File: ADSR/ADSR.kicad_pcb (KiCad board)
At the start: 2 copper layers, 44 parts, among them J1 Panel, J2 Power, Q1 BC547, Q2 BC547, Q3 BC547, U1 LM358, U2 ICM7555

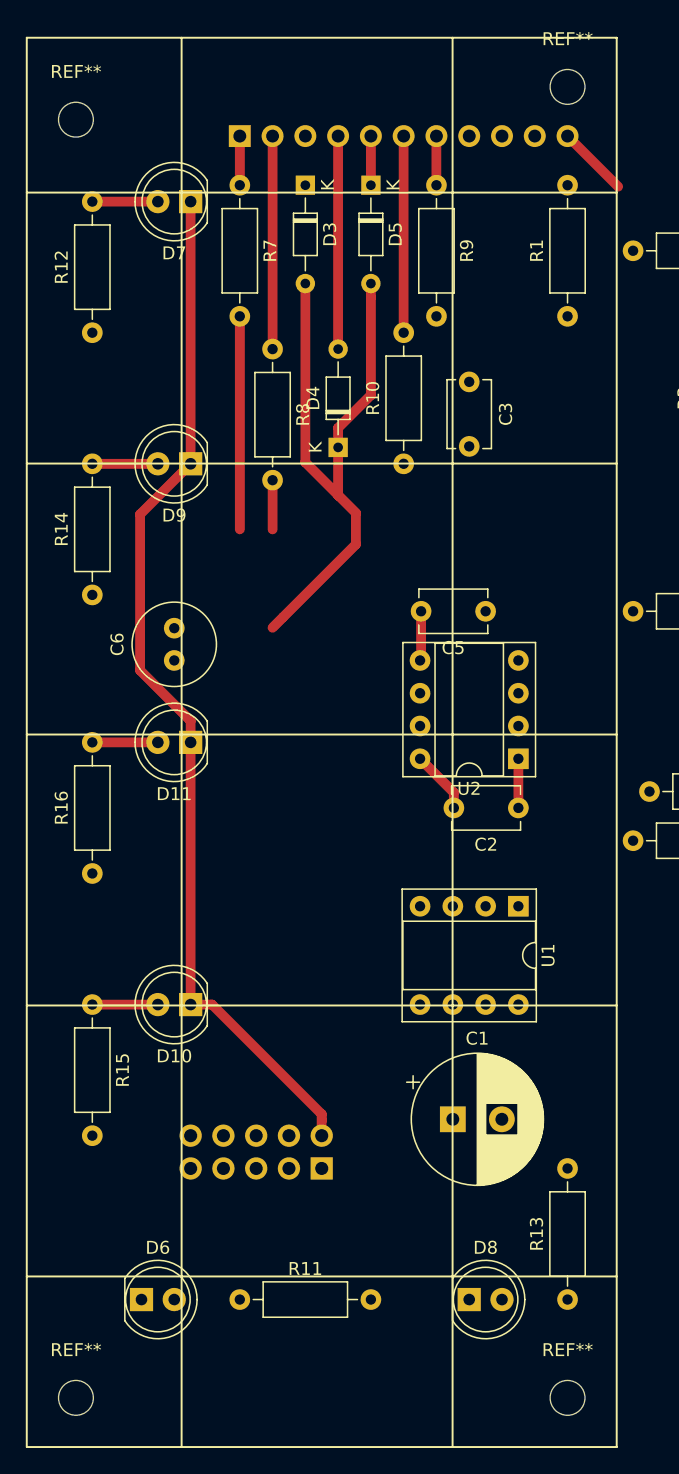
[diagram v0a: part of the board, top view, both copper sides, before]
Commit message: update ADSR footprints
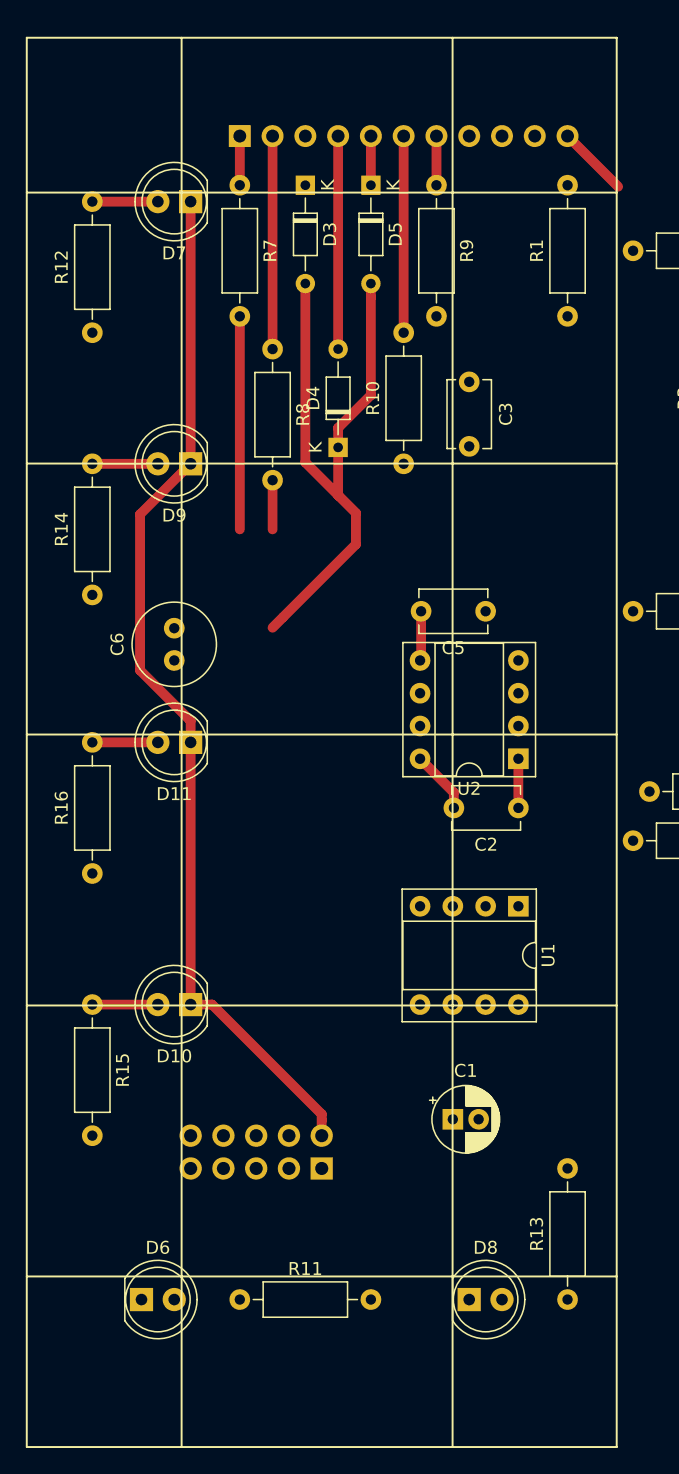
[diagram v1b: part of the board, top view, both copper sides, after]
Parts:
- removed REF** (x4): MountingHole_2.7mm, MountingHole:MountingHole_2.7mm
- C1: footprint Capacitor_THT:CP_Radial_D10.0mm_P3.80mm -> Capacitor_THT:CP_Radial_D5.0mm_P2.00mm
- C6: value 4.7u -> 4u7
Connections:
- C6 pad 1: GND -> Net-(C6-Pad1)
- C6 pad 2: Net-(C6-Pad2) -> GND
- D3 pad 2: Net-(C6-Pad2) -> Net-(C6-Pad1)
- D4 pad 1: Net-(C6-Pad2) -> Net-(C6-Pad1)
- D5 pad 2: Net-(C6-Pad2) -> Net-(C6-Pad1)
- U1 pad 3: Net-(C6-Pad2) -> Net-(C6-Pad1)
- U2 pad 6: Net-(C6-Pad2) -> Net-(C6-Pad1)
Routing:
- net Net-(C6-Pad2): track 48.5 -> 0.00 mm
- net Net-(C6-Pad1): track 0.00 -> 48.5 mm

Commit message: update pcb
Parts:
- added J3: Conn_01x04_Male, Connector_PinHeader_2.54mm:PinHeader_1x04_P2.54mm_Vertical, F.Cu at (139.7, 121.9)
- moved R2 155.5 mm to (113.0, 96.5)
- moved Q1 148.8 mm to (130.8, 104.1)
- moved R13 148.5 mm to (108.0, 97.8), turned to 270 degrees
- moved R4 147.6 mm to (113.0, 92.7)
- moved Q2 147.5 mm to (125.7, 95.2)
- moved R6 146.0 mm to (113.0, 88.9)
- moved R9 144.7 mm to (137.2, 135.9), turned to 180 degrees
- moved Q3 142.3 mm to (127.0, 83.8)
- moved R5 142.3 mm to (128.3, 88.9), turned to 0 degrees
- moved D1 142.3 mm to (137.2, 104.1), turned to 270 degrees
- moved R11 138.8 mm to (108.0, 55.9), turned to 270 degrees
- moved R3 137.8 mm to (133.3, 99.1), turned to 180 degrees
- moved C5 135.9 mm to (111.8, 71.1), turned to 0 degrees
- moved R10 133.5 mm to (128.3, 130.8), turned to 0 degrees
- moved D8 133.5 mm to (115.0, 101.0), turned to 180 degrees
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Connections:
- J1 pad 1: Release_1 -> Release_2
- J1 pad 10: IN -> Net-(J1-Pad10)
- J1 pad 11: OUT -> Net-(J1-Pad11)
- J1 pad 2: Attack_1 -> Attack_2
- J1 pad 3: Release_2 -> Decay_1
- J1 pad 4: Attack_2 -> Sustain_3
- J1 pad 5: Decay_1 -> Release_1
- J1 pad 6: Decay_2 -> Attack_1
- J1 pad 7: Sustain_1 -> IN
- J1 pad 8: Sustain_2 -> Net-(J1-Pad8)
- J1 pad 9: Sustain_3 -> Net-(J1-Pad9)
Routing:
- net Net-(D1-Pad1): track 0.00 -> 47.4 mm
- net +15V: track 4.90 -> 44.5 mm
- net Sustain_3: track 0.00 -> 26.0 mm
- net +5V: track 80.8 -> 106.6 mm
- net Net-(C4-Pad2): track 16.5 -> 41.5 mm
- net Attack_2: track 16.5 -> 0.00 mm
- net Net-(Q3-Pad1): track 0.00 -> 15.4 mm
- net Sustain_2: track 0.00 -> 15.0 mm
- net Sustain_1: track 3.81 -> 16.6 mm
- net Attack_1: track 16.5 -> 3.81 mm
- net Net-(Q1-Pad1): track 0.00 -> 12.4 mm
- net Net-(C4-Pad1): track 0.00 -> 12.0 mm
- net IN: track 0.00 -> 9.20 mm
- net Net-(R10-Pad1): track 0.00 -> 8.89 mm
- net Net-(Q2-Pad2): track 0.00 -> 8.81 mm
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
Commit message: update adsr pcb
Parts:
- removed J3: Conn_01x04_Male, Connector_PinHeader_2.54mm:PinHeader_1x04_P2.54mm_Vertical
- added REF**: MountingHole_2.2mm_M2, MountingHole:MountingHole_2.2mm_M2, F.Cu at (142.2, 53.3)
- added REF**: MountingHole_2.2mm_M2, MountingHole:MountingHole_2.2mm_M2, F.Cu at (102.9, 53.3)
- added REF**: MountingHole_2.2mm_M2, MountingHole:MountingHole_2.2mm_M2, F.Cu at (142.2, 151.1)
- added REF**: MountingHole_2.2mm_M2, MountingHole:MountingHole_2.2mm_M2, F.Cu at (102.9, 151.1)
- R3: footprint Resistor_THT:R_Axial_DIN0207_L6.3mm_D2.5mm_P10.16mm_Horizontal -> Resistor_THT:R_Axial_DIN0207_L6.3mm_D2.5mm_P2.54mm_Vertical
- moved R9 52.7 mm to (123.2, 85.1)
- moved C6 28.1 mm to (109.2, 134.6), turned to 180 degrees
- moved Q1 21.1 mm to (119.4, 121.9)
- moved R16 20.8 mm to (129.5, 134.6), turned to 0 degrees
- moved D1 20.5 mm to (127.0, 121.9), turned to 0 degrees
- moved R3 19.4 mm to (129.5, 118.1)
- moved R1 18.2 mm to (135.9, 85.1)
- moved J1 18.0 mm to (116.8, 71.1)
- moved Q3 18.0 mm to (129.5, 101.6)
- moved R2 18.0 mm to (115.6, 114.3)
- moved R4 18.0 mm to (115.6, 110.5)
- moved R6 18.0 mm to (115.6, 106.7)
- moved C3 17.8 mm to (118.1, 101.6)
- moved D3 17.8 mm to (119.4, 74.9)
- moved D5 17.8 mm to (124.5, 74.9)
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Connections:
- J1 pad 1: Release_2 -> Sustain_3
- J1 pad 10: Net-(J1-Pad10) -> Sustain_2
- J1 pad 11: Net-(J1-Pad11) -> Decay_2
- J1 pad 2: Attack_2 -> Release_2
- J1 pad 3: Decay_1 -> Attack_2
- J1 pad 4: Sustain_3 -> Decay_1
- J1 pad 5: Release_1 -> Sustain_1
- J1 pad 6: Attack_1 -> Release_1
- J1 pad 7: IN -> Attack_1
- J1 pad 8: Net-(J1-Pad8) -> IN
- J1 pad 9: Net-(J1-Pad9) -> OUT
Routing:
- net Sustain_2: track 15.0 -> 82.2 mm
- net OUT: track 8.32 -> 69.9 mm
- net +15V: track 44.5 -> 102.1 mm
- net Decay_2: track 18.2 -> 72.6 mm
- net +5V: track 106.6 -> 160.3 mm
- net Net-(C6-Pad1): track 51.0 -> 63.6 mm
- net Net-(D11-Pad2): track 0.00 -> 8.86 mm
- net Net-(D10-Pad2): track 0.00 -> 5.88 mm
- net IN: track 9.20 -> 4.34 mm
- net Net-(C4-Pad1): track 12.0 -> 7.62 mm
- net Net-(D1-Pad1): track 47.4 -> 51.2 mm
- net Decay_1: track 0.00 -> 3.81 mm
- net Attack_2: track 0.00 -> 3.81 mm
- net Net-(D6-Pad2): track 5.80 -> 8.39 mm
- net Net-(R10-Pad1): track 8.89 -> 6.35 mm
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- added copper zone on B.Cu, net GND

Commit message: update product
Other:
- board outline added: 44.7 x 104.3 mm
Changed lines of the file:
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@@
-(kicad_pcb (version 20171130) (host pcbnew 5.1.2)
+(kicad_pcb (version 20171130) (host pcbnew "(5.0.1)-4")
   (general
     (thickness 1.6)
@@
   )
   (page A4)
+  (title_block
+    (title "The Fastest Envelope in the West")
+    (date 2019-06-10)
+    (rev 1)
+    (company spielhuus)
+    (comment 4 "License CC BY 4.0 - Attribution 4.0 International")
+  )
   (layers
     (0 F.Cu signal)
@@
     (42 Eco1.User user hide)
     (43 Eco2.User user hide)
-    (44 Edge.Cuts user hide)
+    (44 Edge.Cuts user)
     (45 Margin user hide)
     (46 B.CrtYd user hide)
@@
   )
   (setup
-    (last_trace_width 0.762)
+    (last_trace_width 0.25)
     (user_trace_width 0.762)
     (trace_clearance 0.2)
@@
     (zone_45_only no)
     (trace_min 0.2)
+    (segment_width 0.2)
+    (edge_width 0.2)
     (via_size 0.8)
     (via_drill 0.4)
@@
     (uvia_min_size 0.2)
     (uvia_min_drill 0.1)
-    (edge_width 0.1)
-    (segment_width 0.2)
     (pcb_text_width 0.3)
     (pcb_text_size 1.5 1.5)
@@
     )
   )
-  (gr_line (start 100 50) (end 100 154.35) (layer F.SilkS) (width 0.15))
-  (gr_line (start 100 154.35) (end 144.7 154.35) (layer F.SilkS) (width 0.15))
-  (gr_line (start 144.7 50) (end 144.7 154.35) (layer F.SilkS) (width 0.15))
-  (gr_line (start 100 50) (end 144.7 50) (layer F.SilkS) (width 0.15))
+  (gr_line (start 100 50) (end 100 154.35) (layer Edge.Cuts) (width 0.15))
+  (gr_line (start 100 154.35) (end 144.7 154.35) (layer Edge.Cuts) (width 0.15))
+  (gr_line (start 144.7 50) (end 144.7 154.35) (layer Edge.Cuts) (width 0.15))
+  (gr_line (start 100 50) (end 144.7 50) (layer Edge.Cuts) (width 0.15))
   (segment (start 118.11 97.79) (end 119.38 96.52) (width 0.762) (layer B.Cu) (net 2))
   (segment (start 118.11 101.6) (end 118.11 97.79) (width 0.762) (layer B.Cu) (net 2))

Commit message: update pcb
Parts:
- added G***: LOGO, logo:spielhuus, F.Cu at (134.6, 62.2)
- moved R10 14.8 mm to (127.0, 125.7)
- moved C1 14.4 mm to (132.1, 133.3)
- moved R16 13.0 mm to (142.2, 137.2), turned to 270 degrees
- moved J2 7.62 mm to (129.5, 143.5)
- moved D11 7.00 mm to (134.6, 149.9)
- moved D10 6.86 mm to (115.0, 149.9)
- moved REF** 0.87 mm to (102.5, 52.5)
- moved REF** 0.80 mm to (142.2, 52.5)
- moved REF** 0.76 mm to (102.5, 151.8)
- moved REF** 0.68 mm to (142.2, 151.8)
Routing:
- net +15V: track 102.1 -> 133.4 mm
- net +5V: track 160.3 -> 180.5 mm
- net Decay_2: track 72.6 -> 56.7 mm
- net GND: track 0.00 -> 10.0 mm
- net Net-(R10-Pad1): track 6.35 -> 14.6 mm
- net Net-(D10-Pad2): track 5.88 -> 12.0 mm
- net OUT: track 69.9 -> 64.8 mm
- net Net-(D11-Pad2): track 8.86 -> 6.13 mm
- net Sustain_2: track 82.2 -> 81.2 mm
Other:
- board text added: "ADSR"
- board text added: "REV01"

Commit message: update vco1 pcb
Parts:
- moved D9 2.84 mm to (114.3, 120.7), turned to 180 degrees
- moved D6 2.63 mm to (114.3, 59.7), turned to 180 degrees
- moved D8 2.63 mm to (114.3, 100.3), turned to 180 degrees
- moved D7 2.54 mm to (114.3, 80.0), turned to 180 degrees
- moved D11 2.54 mm to (137.2, 149.9), turned to 180 degrees
- moved D10 1.97 mm to (113.0, 149.9), turned to 0 degrees
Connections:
- D10 pad 1: +5V -> Net-(D10-Pad1)
- D10 pad 2: Net-(D10-Pad2) -> +5V
- D11 pad 1: +5V -> Net-(D11-Pad1)
- D11 pad 2: Net-(D11-Pad2) -> +5V
- D6 pad 1: +5V -> Net-(D6-Pad1)
- D6 pad 2: Net-(D6-Pad2) -> +5V
- D7 pad 1: +5V -> Net-(D7-Pad1)
- D7 pad 2: Net-(D7-Pad2) -> +5V
- D8 pad 1: +5V -> Net-(D8-Pad1)
- D8 pad 2: Net-(D8-Pad2) -> +5V
- D9 pad 1: +5V -> Net-(D9-Pad1)
- D9 pad 2: Net-(D9-Pad2) -> +5V
- R11 pad 1: Net-(D6-Pad2) -> Net-(D6-Pad1)
- R12 pad 2: Net-(D7-Pad2) -> Net-(D7-Pad1)
- R13 pad 1: Net-(D8-Pad2) -> Net-(D8-Pad1)
- R14 pad 2: Net-(D9-Pad2) -> Net-(D9-Pad1)
- R15 pad 1: Net-(D10-Pad2) -> Net-(D10-Pad1)
- R16 pad 2: Net-(D11-Pad2) -> Net-(D11-Pad1)
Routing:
- net +5V: track 180.5 -> 164.7 mm
- net Net-(D10-Pad2): track 12.0 -> 0.00 mm
- net Net-(D10-Pad1): track 0.00 -> 12.0 mm
- net Net-(D9-Pad1): track 0.00 -> 8.90 mm
- net Net-(D8-Pad1): track 0.00 -> 8.90 mm
- net Net-(D6-Pad2): track 8.39 -> 0.00 mm
- net Net-(D6-Pad1): track 0.00 -> 8.39 mm
- net Net-(D7-Pad2): track 8.28 -> 0.00 mm
- net Net-(D7-Pad1): track 0.00 -> 8.28 mm
- net Net-(D9-Pad2): track 8.15 -> 0.00 mm
- net Net-(D8-Pad2): track 7.90 -> 0.00 mm
- net Net-(D11-Pad2): track 6.13 -> 0.00 mm
- net Net-(D11-Pad1): track 0.00 -> 6.13 mm

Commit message: check pcb
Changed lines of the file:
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@@
-(kicad_pcb (version 20171130) (host pcbnew 5.1.2)
+(kicad_pcb (version 20171130) (host pcbnew "(5.0.1)-4")
   (general
     (thickness 1.6)
@@
   (layers
     (0 F.Cu signal)
-    (31 B.Cu signal)
+    (31 B.Cu signal hide)
     (32 B.Adhes user)
     (33 F.Adhes user)
@@
   )
   (setup
-    (last_trace_width 0.762)
+    (last_trace_width 0.25)
     (user_trace_width 0.762)
     (trace_clearance 0.2)
@@
     (zone_45_only no)
     (trace_min 0.2)
+    (segment_width 0.2)
+    (edge_width 0.2)
     (via_size 0.8)
     (via_drill 0.4)
@@
     (uvia_min_size 0.2)
     (uvia_min_drill 0.1)
-    (edge_width 0.2)
-    (segment_width 0.2)
     (pcb_text_width 0.3)
     (pcb_text_size 1.5 1.5)
@@
     (fp_circle (center 0 0) (end 2.45 0) (layer F.CrtYd) (width 0.05))
     (fp_circle (center 0 0) (end 2.2 0) (layer Cmts.User) (width 0.15))
-    (fp_text user %R (at 0.3 0) (layer F.Fab)
+    (fp_text user %R (at 0.3 0) (layer F.Fab) hide
       (effects (font (size 1 1) (thickness 0.15)))
     )
@@
     (tags "mounting hole 2.2mm no annular m2")
     (attr virtual)
-    (fp_text reference REF** (at 0 2.54) (layer F.SilkS)
+    (fp_text reference REF** (at 0 2.54) (layer F.SilkS) hide
       (effects (font (size 1 1) (thickness 0.15)))
     )
@@
     (fp_circle (center 0 0) (end 2.45 0) (layer F.CrtYd) (width 0.05))
     (fp_circle (center 0 0) (end 2.2 0) (layer Cmts.User) (width 0.15))
-    (fp_text user %R (at 0.3 0) (layer F.Fab)
+    (fp_text user %R (at 0.3 0) (layer F.Fab) hide
       (effects (font (size 1 1) (thickness 0.15)))
     )
@@
       (effects (font (size 1 1) (thickness 0.15)))
     )
-    (fp_text user %R (at 0.3 0) (layer F.Fab)
+    (fp_text user %R (at 0.3 0) (layer F.Fab) hide
       (effects (font (size 1 1) (thickness 0.15)))
     )
@@
     (fp_circle (center 0 0) (end 2.45 0) (layer F.CrtYd) (width 0.05))
     (fp_circle (center 0 0) (end 2.2 0) (layer Cmts.User) (width 0.15))
-    (fp_text user %R (at 0.3 0) (layer F.Fab)
+    (fp_text user %R (at 0.3 0) (layer F.Fab) hide
       (effects (font (size 1 1) (thickness 0.15)))
     )
@@
     (descr "LED, Round, FlatTop, diameter 5.0mm, 2 pins, http://www.kingbright.com/attachments/file/psearch/000/00/00/L-483GDT(Ver.15B).pdf")
     (tags "LED Round FlatTop diameter 5.0mm 2 pins")
-    (fp_text reference D11 (at 2.54 -4.01) (layer F.SilkS)
+    (fp_text reference D11 (at 6.35 -2.54) (layer F.SilkS)
       (effects (font (size 1 1) (thickness 0.15)))
     )
@@
     (descr "LED, Round, FlatTop, diameter 5.0mm, 2 pins, http://www.kingbright.com/attachments/file/psearch/000/00/00/L-483GDT(Ver.15B).pdf")
     (tags "LED Round FlatTop diameter 5.0mm 2 pins")
-    (fp_text reference D10 (at 2.81 4.42) (layer F.SilkS)
+    (fp_text reference D10 (at 6.35 2.54) (layer F.SilkS)
       (effects (font (size 1 1) (thickness 0.15)))
     )
@@
   (segment (start 119.38 133.35) (end 119.38 134.62) (width 0.762) (layer B.Cu) (net 26) (status 20))
   (segment (start 127 125.73) (end 119.38 133.35) (width 0.762) (layer B.Cu) (net 26) (status 10))
-  (segment (start 114.3 57.727208) (end 114.3 59) (width 0.762) (layer B.Cu) (net 28) (status 20))
-  (segment (start 112.452792 55.88) (end 114.3 57.727208) (width 0.762) (layer B.Cu) (net 28))
-  (segment (start 107.95 55.88) (end 112.452792 55.88) (width 0.762) (layer B.Cu) (net 28) (status 10))
-  (segment (start 108.749999 77.940001) (end 107.95 78.74) (width 0.762) (layer B.Cu) (net 29) (status 30))
-  (segment (start 113.512793 77.940001) (end 108.749999 77.940001) (width 0.762) (layer B.Cu) (net 29) (status 20))
-  (segment (start 114.3 80) (end 114.3 78.727208) (width 0.762) (layer B.Cu) (net 29) (status 10))
-  (segment (start 114.3 78.727208) (end 113.512793 77.940001) (width 0.762) (layer B.Cu) (net 29))
-  (segment (start 107.95 145.35) (end 107.95 139.7) (width 0.762) (layer F.Cu) (net 32) (status 20))
-  (segment (start 112.46 149.86) (end 107.95 145.35) (width 0.762) (layer F.Cu) (net 32) (status 10))
-  (segment (start 139.7 149.86) (end 142.24 147.32) (width 0.762) (layer F.Cu) (net 33) (status 20))
-  (segment (start 137.16 149.86) (end 139.7 149.86) (width 0.762) (layer F.Cu) (net 33) (status 10))
   (segment (start 119.38 82.55) (end 124.46 82.55) (width 0.762) (layer B.Cu) (net 27) (status 30))
   (segment (start 120.761001 90.058999) (end 120.179999 90.640001) (width 0.762) (layer B.Cu) (net 27) (status 20))
@@
   (segment (start 120.761001 92.821001) (end 120.761001 117.908513) (width 0.762) (layer B.Cu) (net 27))
   (segment (start 119.38 91.44) (end 120.761001 92.821001) (width 0.762) (layer B.Cu) (net 27) (status 10))
+  (segment (start 114.3 57.727208) (end 114.3 59) (width 0.762) (layer B.Cu) (net 28) (status 20))
+  (segment (start 112.452792 55.88) (end 114.3 57.727208) (width 0.762) (layer B.Cu) (net 28))
+  (segment (start 107.95 55.88) (end 112.452792 55.88) (width 0.762) (layer B.Cu) (net 28) (status 10))
+  (segment (start 108.749999 77.940001) (end 107.95 78.74) (width 0.762) (layer B.Cu) (net 29) (status 30))
+  (segment (start 113.512793 77.940001) (end 108.749999 77.940001) (width 0.762) (layer B.Cu) (net 29) (status 20))
+  (segment (start 114.3 80) (end 114.3 78.727208) (width 0.762) (layer B.Cu) (net 29) (status 10))
+  (segment (start 114.3 78.727208) (end 113.512793 77.940001) (width 0.762) (layer B.Cu) (net 29))
   (segment (start 114.3 98.668) (end 114.3 100.33) (width 0.762) (layer B.Cu) (net 30))
   (segment (start 109.22 97.79) (end 113.422 97.79) (width 0.762) (layer B.Cu) (net 30))
@@
   (segment (start 109.22 118.11) (end 113.422 118.11) (width 0.762) (layer B.Cu) (net 31))
   (segment (start 107.95 119.38) (end 109.22 118.11) (width 0.762) (layer B.Cu) (net 31))
+  (segment (start 107.95 145.35) (end 107.95 139.7) (width 0.762) (layer F.Cu) (net 32) (status 20))
+  (segment (start 112.46 149.86) (end 107.95 145.35) (width 0.762) (layer F.Cu) (net 32) (status 10))
+  (segment (start 139.7 149.86) (end 142.24 147.32) (width 0.762) (layer F.Cu) (net 33) (status 20))
+  (segment (start 137.16 149.86) (end 139.7 149.86) (width 0.762) (layer F.Cu) (net 33) (status 10))
   (zone (net 1) (net_name GND) (layer B.Cu) (hatch edge 0.508)
     (connect_pads (clearance 0.508))
